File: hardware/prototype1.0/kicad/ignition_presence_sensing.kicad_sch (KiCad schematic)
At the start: 5 parts

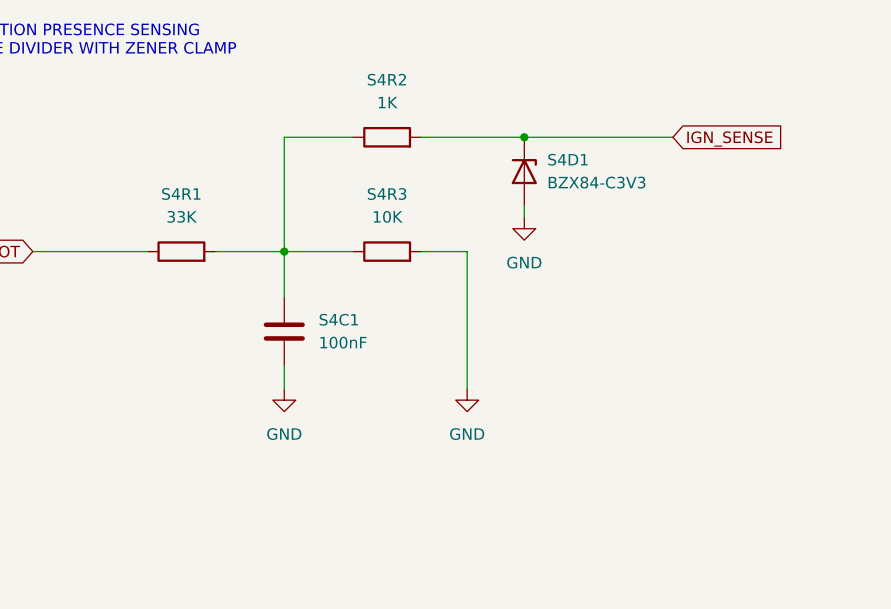
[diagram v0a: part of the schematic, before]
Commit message: updated the ignition sensing voltage divider and added a 4.2 buck to power the ConnectKit board
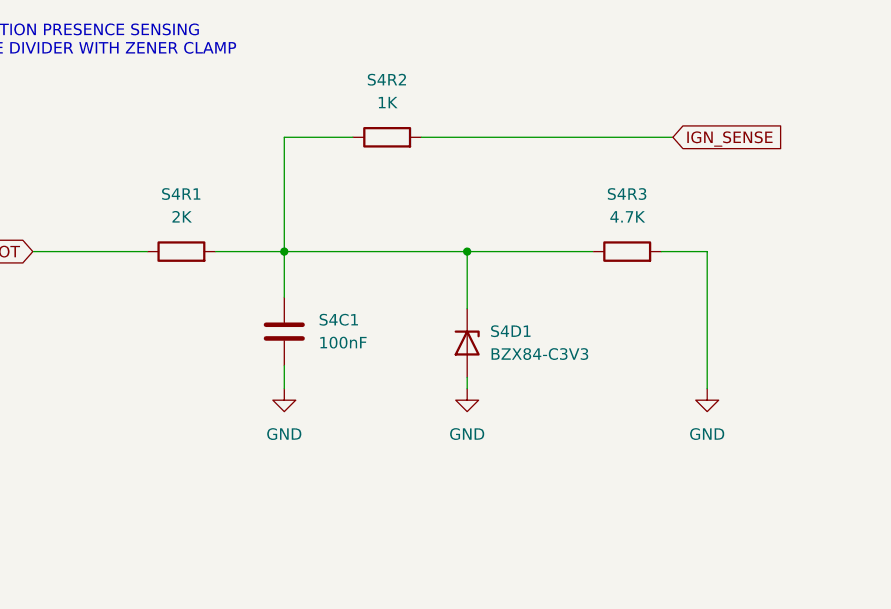
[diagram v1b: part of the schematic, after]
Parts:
- S4R1: value 33K -> 2K
- S4R3: value 10K -> 4.7K
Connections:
- net IGN_SENSE: no longer S4D1.3 (K)
- net at S4C1.1, S4R1.2, S4R2.1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: now also S4D1.3 (K)
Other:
- moved on the sheet: S4D1, S4R3
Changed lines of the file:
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@@
 	)
 	(junction
-		(at 93.98 40.64)
+		(at 87.63 53.34)
 		(diameter 0)
 		(color 0 0 0 0)
@@
 	(wire
 		(pts
-			(xy 87.63 68.58) (xy 87.63 53.34)
-		)
-		(stroke
-			(width 0)
-			(type default)
-		)
-	)
-	(wire
-		(pts
-			(xy 93.98 48.26) (xy 93.98 49.53)
+			(xy 114.3 68.58) (xy 114.3 53.34)
+		)
+		(stroke
+			(width 0)
+			(type default)
+		)
+	)
+	(wire
+		(pts
+			(xy 87.63 67.31) (xy 87.63 68.58)
 		)
 		(stroke
@@
 	(wire
 		(pts
-			(xy 82.55 53.34) (xy 87.63 53.34)
-		)
-		(stroke
-			(width 0)
-			(type default)
-		)
-	)
-	(wire
-		(pts
-			(xy 82.55 40.64) (xy 93.98 40.64)
+			(xy 109.22 53.34) (xy 114.3 53.34)
 		)
 		(stroke
@@
 	(wire
 		(pts
-			(xy 93.98 40.64) (xy 110.49 40.64)
+			(xy 82.55 40.64) (xy 110.49 40.64)
 		)
 		(stroke
@@
 	(wire
 		(pts
-			(xy 67.31 53.34) (xy 74.93 53.34)
+			(xy 87.63 53.34) (xy 87.63 59.69)
+		)
+		(stroke
+			(width 0)
+			(type default)
+		)
+	)
+	(wire
+		(pts
+			(xy 67.31 53.34) (xy 87.63 53.34)
+		)
+		(stroke
+			(width 0)
+			(type default)
+		)
+	)
+	(wire
+		(pts
+			(xy 87.63 53.34) (xy 101.6 53.34)
 		)
 		(stroke
@@
 	(symbol
 		(lib_id "Diode:BZX84Cxx")
-		(at 93.98 44.45 270)
+		(at 87.63 63.5 270)
 		(unit 1)
 		(body_style 1)
@@
 		(fields_autoplaced yes)
 		(property "Reference" "S4D1"
-			(at 96.52 43.1799 90)
+			(at 90.17 62.2299 90)
 			(show_name no)
 			(do_not_autoplace no)
@@
 		)
 		(property "Value" "BZX84-C3V3"
-			(at 96.52 45.7199 90)
+			(at 90.17 64.7699 90)
 			(show_name no)
 			(do_not_autoplace no)
@@
 		)
 		(property "Footprint" "Package_TO_SOT_SMD:SOT-23"
-			(at 93.98 44.45 0)
+			(at 87.63 63.5 0)
 			(hide yes)
 			(show_name no)
@@
 		)
 		(property "Datasheet" "https://diotec.com/tl_files/diotec/files/pdf/datasheets/bzx84c2v4.pdf"
-			(at 93.98 44.45 0)
+			(at 87.63 63.5 0)
 			(hide yes)
 			(show_name no)
@@
 		)
 		(property "Description" "300mW Zener Diode, SOT-23"
-			(at 93.98 44.45 0)
+			(at 87.63 63.5 0)
 			(hide yes)
 			(show_name no)
@@
 	(symbol
 		(lib_id "Device:R")
-		(at 78.74 53.34 90)
+		(at 105.41 53.34 90)
 		(unit 1)
 		(body_style 1)
@@
 		(fields_autoplaced yes)
 		(property "Reference" "S4R3"
-			(at 78.74 46.99 90)
-			(show_name no)
-			(do_not_autoplace no)
-			(effects
-				(font
-					(size 1.27 1.27)
-				)
-			)
-		)
-		(property "Value" "10K"
-			(at 78.74 49.53 90)
+			(at 105.41 46.99 90)
+			(show_name no)
+			(do_not_autoplace no)
+			(effects
+				(font
+					(size 1.27 1.27)
+				)
+			)
+		)
+		(property "Value" "4.7K"
+			(at 105.41 49.53 90)
 			(show_name no)
 			(do_not_autoplace no)
@@
 		)
 		(property "Footprint" "Resistor_SMD:R_0402_1005Metric"
-			(at 78.74 55.118 90)
+			(at 105.41 55.118 90)
 			(hide yes)
 			(show_name no)
@@
 		)
 		(property "Datasheet" ""
-			(at 78.74 53.34 0)
+			(at 105.41 53.34 0)
 			(hide yes)
 			(show_name no)
@@
 		)
 		(property "Description" "Resistor"
-			(at 78.74 53.34 0)
+			(at 105.41 53.34 0)
 			(hide yes)
 			(show_name no)
@@
 			)
 		)
-		(property "Value" "33K"
+		(property "Value" "2K"
 			(at 55.88 49.53 90)
 			(show_name no)
@@
 				(path "/9f6f029d-c66b-4815-8da3-518accca920f"
 					(reference "S4R1")
+					(unit 1)
+				)
+			)
+		)
+	)
+	(symbol
+		(lib_id "power:GND")
+		(at 114.3 68.58 0)
+		(unit 1)
+		(body_style 1)
+		(exclude_from_sim no)
+		(in_bom yes)
+		(on_board yes)
+		(in_pos_files yes)
+		(dnp no)
+		(fields_autoplaced yes)
+		(property "Reference" "#PWR010"
+			(at 114.3 74.93 0)
+			(hide yes)
+			(show_name no)
+			(do_not_autoplace no)
+			(effects
+				(font
+					(size 1.27 1.27)
+				)
+			)
+		)
+		(property "Value" "GND"
+			(at 114.3 73.66 0)
+			(show_name no)
+			(do_not_autoplace no)
+			(effects
+				(font
+					(size 1.27 1.27)
+				)
+			)
+		)
+		(property "Footprint" ""
+			(at 114.3 68.58 0)
+			(hide yes)
+			(show_name no)
+			(do_not_autoplace no)
+			(effects
+				(font
+					(size 1.27 1.27)
+				)
+			)
+		)
+		(property "Datasheet" ""
+			(at 114.3 68.58 0)
+			(hide yes)
+			(show_name no)
+			(do_not_autoplace no)
+			(effects
+				(font
+					(size 1.27 1.27)
+				)
+			)
+		)
+		(property "Description" "Power symbol creates a global label with name \"GND\" , ground"
+			(at 114.3 68.58 0)
+			(hide yes)
+			(show_name no)
+			(do_not_autoplace no)
+			(effects
+				(font
+					(size 1.27 1.27)
+				)
+			)
+		)
+		(pin "1"
+		)
+		(instances
+			(project "l0destar"
+				(path "/9f6f029d-c66b-4815-8da3-518accca920f"
+					(reference "#PWR010")
 					(unit 1)
 				)
@@
 		(dnp no)
 		(fields_autoplaced yes)
-		(property "Reference" "#PWR010"
+		(property "Reference" "#PWR015"
 			(at 87.63 74.93 0)
 			(hide yes)
@@
 			(hide yes)
 			(show_name no)
-			(do_not_autoplace no)
-			(effects
-				(font
-					(size 1.27 1.27)
-				)
-			)
-		)
-		(pin "1"
-		)
-		(instances
-			(project "l0destar"
-				(path "/9f6f029d-c66b-4815-8da3-518accca920f"
-					(reference "#PWR010")
-					(unit 1)
-				)
-			)
-		)
-	)
-	(symbol
-		(lib_id "power:GND")
-		(at 93.98 49.53 0)
-		(unit 1)
-		(body_style 1)
-		(exclude_from_sim no)
-		(in_bom yes)
-		(on_board yes)
-		(in_pos_files yes)
-		(dnp no)
-		(fields_autoplaced yes)
-		(property "Reference" "#PWR015"
-			(at 93.98 55.88 0)
-			(hide yes)
-			(show_name no)
-			(do_not_autoplace no)
-			(effects
-				(font
-					(size 1.27 1.27)
-				)
-			)
-		)
-		(property "Value" "GND"
-			(at 93.98 54.61 0)
-			(show_name no)
-			(do_not_autoplace no)
-			(effects
-				(font
-					(size 1.27 1.27)
-				)
-			)
-		)
-		(property "Footprint" ""
-			(at 93.98 49.53 0)
-			(hide yes)
-			(show_name no)
-			(do_not_autoplace no)
-			(effects
-				(font
-					(size 1.27 1.27)
-				)
-			)
-		)
-		(property "Datasheet" ""
-			(at 93.98 49.53 0)
-			(hide yes)
-			(show_name no)
-			(do_not_autoplace no)
-			(effects
-				(font
-					(size 1.27 1.27)
-				)
-			)
-		)
-		(property "Description" "Power symbol creates a global label with name \"GND\" , ground"
-			(at 93.98 49.53 0)
-			(hide yes)
-			(show_name no)

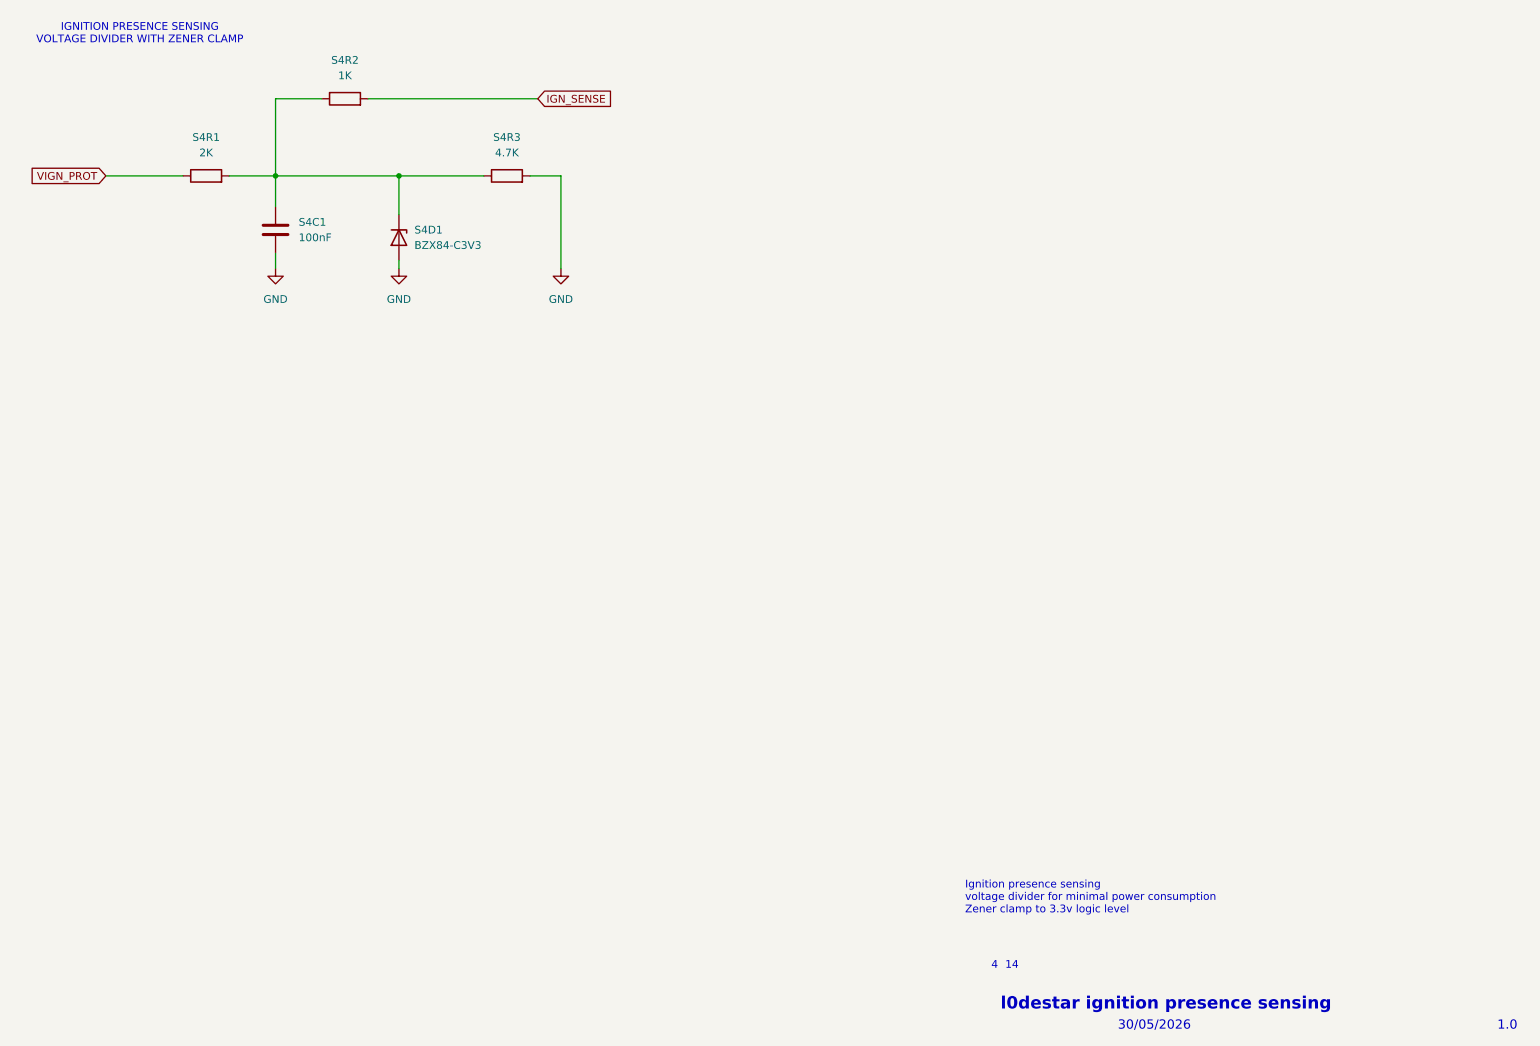
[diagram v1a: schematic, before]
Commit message: replaced the voltage divider that derives the ignition signal with a MOSFET gating the 3.3v rail
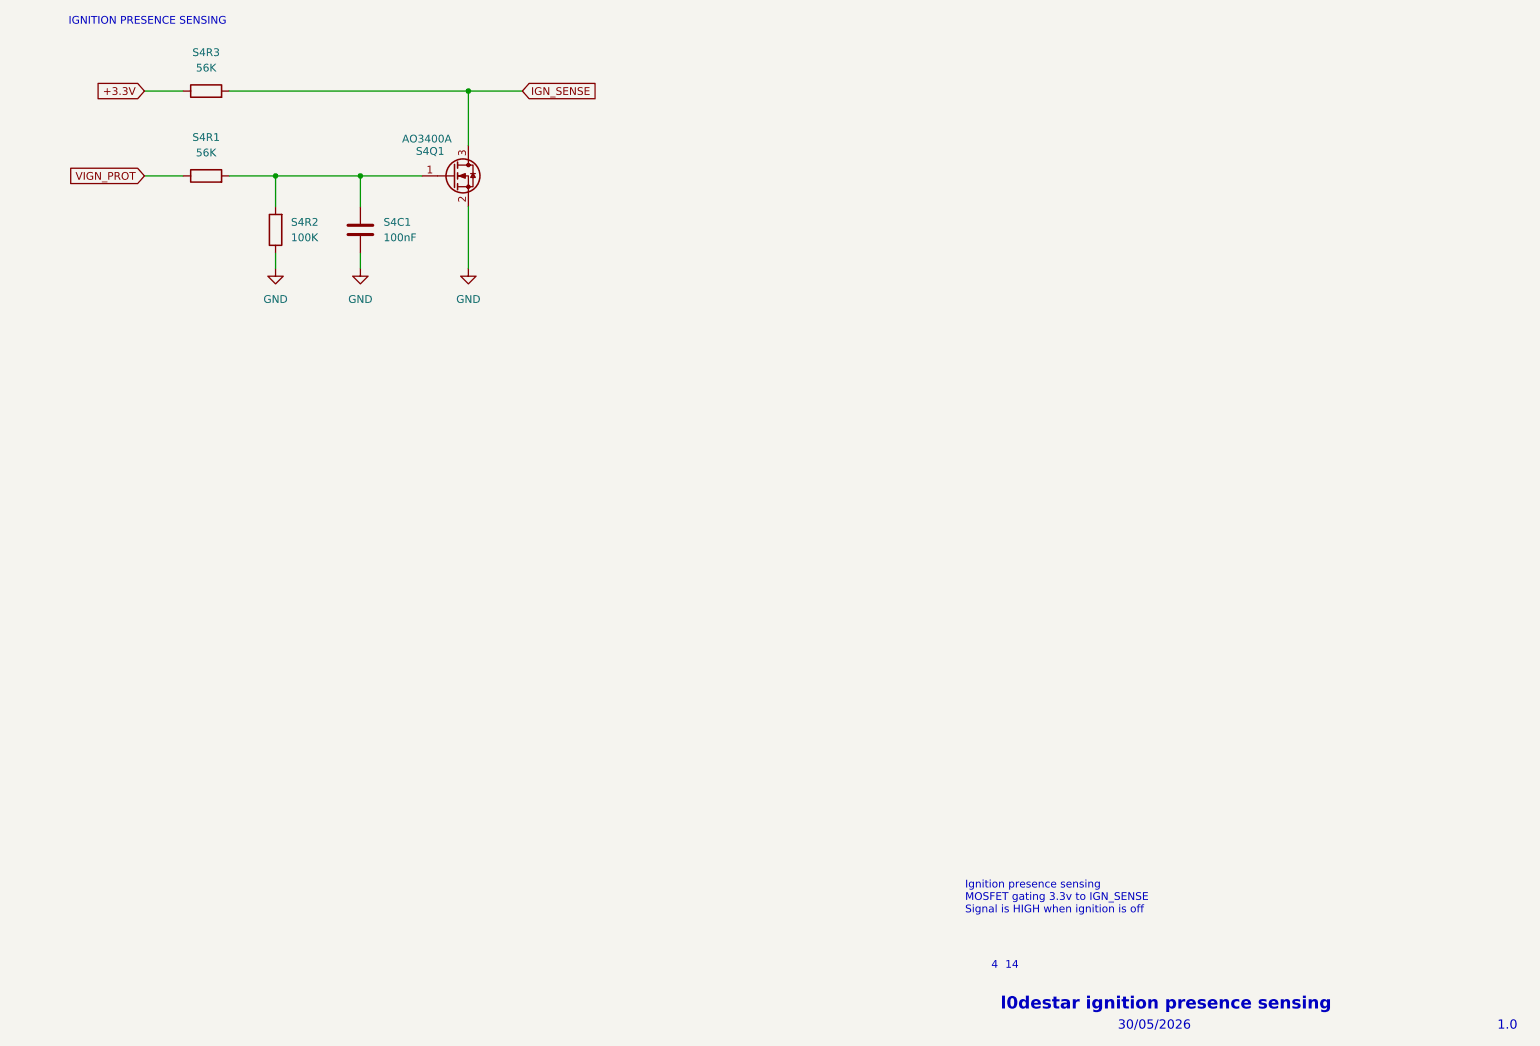
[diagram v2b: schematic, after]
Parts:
- removed S4D1: BZX84-C3V3, Package_TO_SOT_SMD:SOT-23, symbol Diode:BZX84Cxx
- added S4Q1: AO3400A, Package_TO_SOT_SMD:SOT-23, symbol Transistor_FET:AO3400A
- S4R1: value 2K -> 56K
- S4R2: value 1K -> 100K
- S4R3: value 4.7K -> 56K
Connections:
- net GND: now also S4R2.1, S4Q1.2 (S); no longer S4R3.2
- net IGN_SENSE: now also S4R3.2, S4Q1.3 (D); no longer S4R2.2
- net at S4C1.1, S4R1.2: now also S4R2.2, S4Q1.1 (G); no longer S4R2.1, S4R3.1
- new net +3.3V: S4R3.1
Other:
- note added: "IGNITION PRESENCE SENSING"
- note added: "Ignition presence sensing MOSFET gating 3.3v to IGN_SENSE Signal is HIGH when ignition is off"
- note removed: "IGNITION PRESENCE SENSING VOLTAGE DIVIDER WITH ZENER CLAMP"
- note removed: "Ignition presence sensing voltage divider for minimal power consumption Zener clamp to 3.3v logic level"
- moved on the sheet: S4C1, S4R2, S4R3
